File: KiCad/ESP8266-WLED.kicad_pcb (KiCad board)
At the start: 2 copper layers, 25.3 x 35.8 mm, 10 parts, among them J1 USB_C_Receptacle_USB2.0_14P, U1 ESP-12F

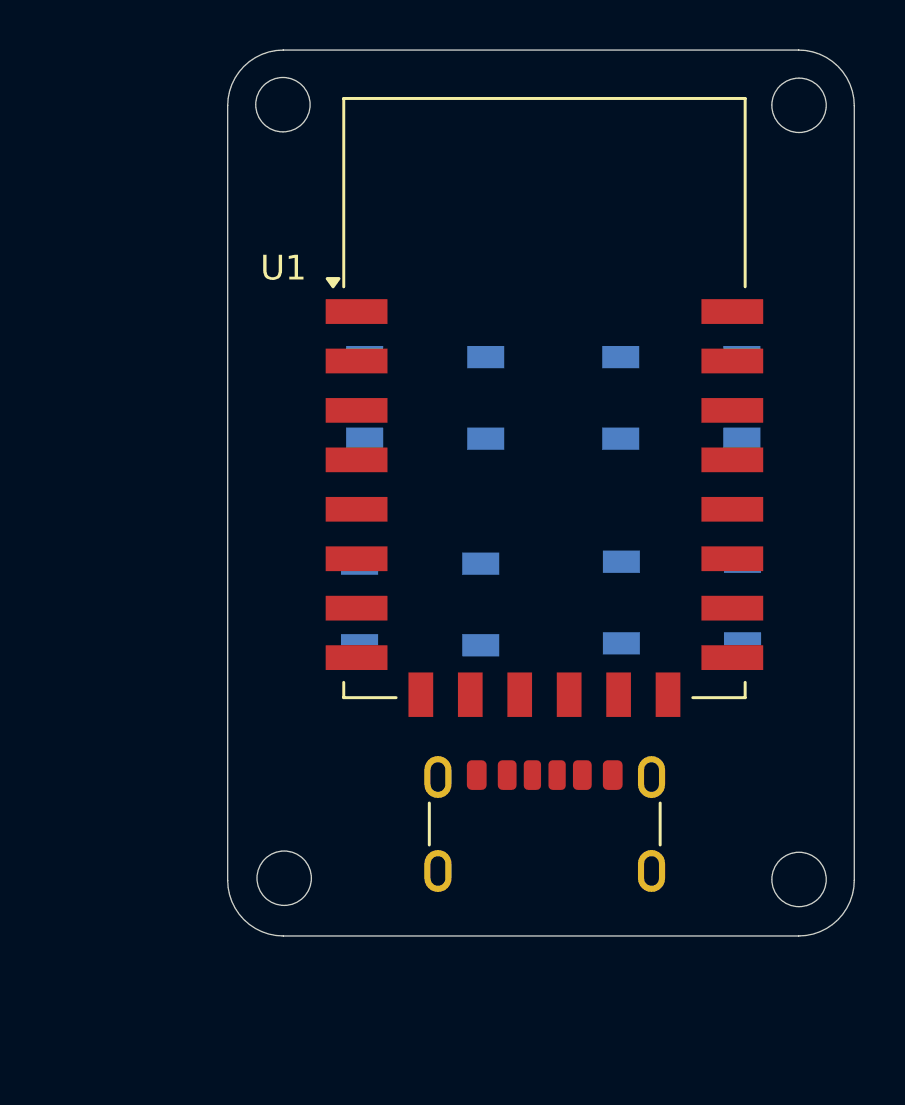
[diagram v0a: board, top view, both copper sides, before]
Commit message: adding power supply, etc.
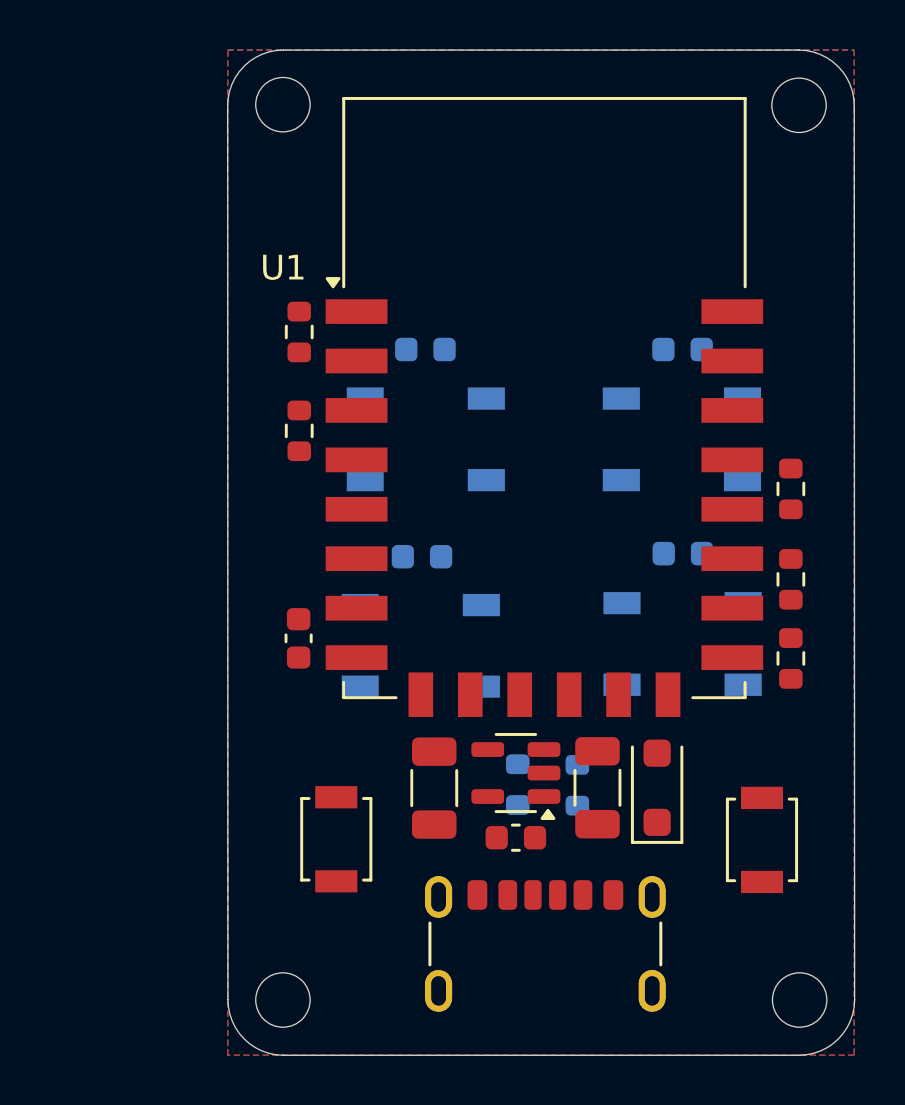
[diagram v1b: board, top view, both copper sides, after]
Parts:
- added C1: 100nF, Capacitor_SMD:C_0603_1608Metric, F.Cu at (140.1, 107.6)
- added C2: 100nF, Capacitor_SMD:C_0603_1608Metric, B.Cu at (155.6, 95.9)
- added C3: 100nF, Capacitor_SMD:C_0603_1608Metric, B.Cu at (155.6, 104.2)
- added C4: 100nF, Capacitor_SMD:C_0603_1608Metric, B.Cu at (145.0, 104.3)
- added C5: 100nF, Capacitor_SMD:C_0603_1608Metric, B.Cu at (145.2, 95.9)
- added C6: 10u, Capacitor_SMD:C_1206_3216Metric, F.Cu at (152.1, 113.6)
- added C7: 10u, Capacitor_SMD:C_1206_3216Metric, F.Cu at (145.5, 113.7)
- added C8: 470pF, Capacitor_SMD:C_0603_1608Metric, F.Cu at (148.8, 115.7)
- added D5: MBR120VLSFT1G, Diode_SMD:D_SOD-123F, F.Cu at (154.6, 113.6)
- added R1: 10K, Resistor_SMD:R_0603_1608Metric, F.Cu at (140.1, 95.2)
- added R2: 10K, Resistor_SMD:R_0603_1608Metric, F.Cu at (140.1, 99.2)
- added R3: 10K, Resistor_SMD:R_0603_1608Metric, F.Cu at (160.0, 101.5)
- added R4: 10K, Resistor_SMD:R_0603_1608Metric, F.Cu at (160.0, 105.2)
- added R5: 10K, Resistor_SMD:R_0603_1608Metric, F.Cu at (160.0, 108.4)
- added R6: 5k1, Resistor_SMD:R_0603_1608Metric, B.Cu at (148.9, 113.5)
- added R7: 5k1, Resistor_SMD:R_0603_1608Metric, B.Cu at (151.3, 113.5)
- added SW1: SW_Push, Button_Switch_SMD:SW_SPST_B3U-1000P, F.Cu at (141.6, 115.7)
- added SW2: SW_Push, Button_Switch_SMD:SW_SPST_B3U-1000P, F.Cu at (158.8, 115.7)
- added U2: MIC5219-3.3YM5, Package_TO_SOT_SMD:SOT-23-5, F.Cu at (148.8, 113.0)
- moved REF** 4.93 mm to (139.4, 122.2)
- moved REF** 4.88 mm to (160.3, 122.2)
- moved J1 4.85 mm to (150.0, 121.1)
- moved D1 1.68 mm to (155.6, 99.5)
- moved D4 1.68 mm to (145.0, 107.9)
- moved D2 1.68 mm to (145.2, 99.5)
- moved D3 1.68 mm to (155.6, 107.8)
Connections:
- D1 pad 1: unconnected-(D1-VDD-Pad1) -> +5V
- D1 pad 2: unconnected-(D1-DOUT-Pad2) -> Net-(D1-DOUT)
- D1 pad 3: unconnected-(D1-VSS-Pad3) -> GND
- D2 pad 1: unconnected-(D2-VDD-Pad1) -> +5V
- D2 pad 2: unconnected-(D2-DOUT-Pad2) -> Net-(D2-DOUT)
- D2 pad 3: unconnected-(D2-VSS-Pad3) -> GND
- D2 pad 4: unconnected-(D2-DIN-Pad4) -> Net-(D1-DOUT)
- D3 pad 1: unconnected-(D3-VDD-Pad1) -> +5V
- D3 pad 2: unconnected-(D3-DOUT-Pad2) -> Net-(D3-DOUT)
- D3 pad 3: unconnected-(D3-VSS-Pad3) -> GND
- D3 pad 4: unconnected-(D3-DIN-Pad4) -> Net-(D2-DOUT)
- D4 pad 1: unconnected-(D4-VDD-Pad1) -> +5V
- D4 pad 3: unconnected-(D4-VSS-Pad3) -> GND
- D4 pad 4: unconnected-(D4-DIN-Pad4) -> Net-(D3-DOUT)
- J1 pad A12: Net-(J1-GND-PadA1) -> GND
- J1 pad A5: unconnected-(J1-CC1-PadA5) -> Net-(J1-CC1)
- J1 pad B12: Net-(J1-GND-PadA1) -> GND
- J1 pad B5: unconnected-(J1-CC2-PadB5) -> Net-(J1-CC2)
- J1 pad S1: unconnected-(J1-SHIELD-PadS1) -> GND
- U1 pad 1: unconnected-(U1-~{RST}-Pad1) -> Net-(U1-~{RST})
- U1 pad 16: unconnected-(U1-GPIO15-Pad16) -> Net-(U1-GPIO15)
- U1 pad 17: unconnected-(U1-GPIO2-Pad17) -> Net-(U1-GPIO2)
- U1 pad 18: unconnected-(U1-GPIO0-Pad18) -> Net-(U1-GPIO0)
- U1 pad 3: unconnected-(U1-EN-Pad3) -> Net-(U1-EN)
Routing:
- added copper zone on B.Cu, net GND
- added copper zone on F.Cu, net GND
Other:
- board size 25.3 x 35.8 mm -> 25.4 x 40.7 mm

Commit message: adding serial interface
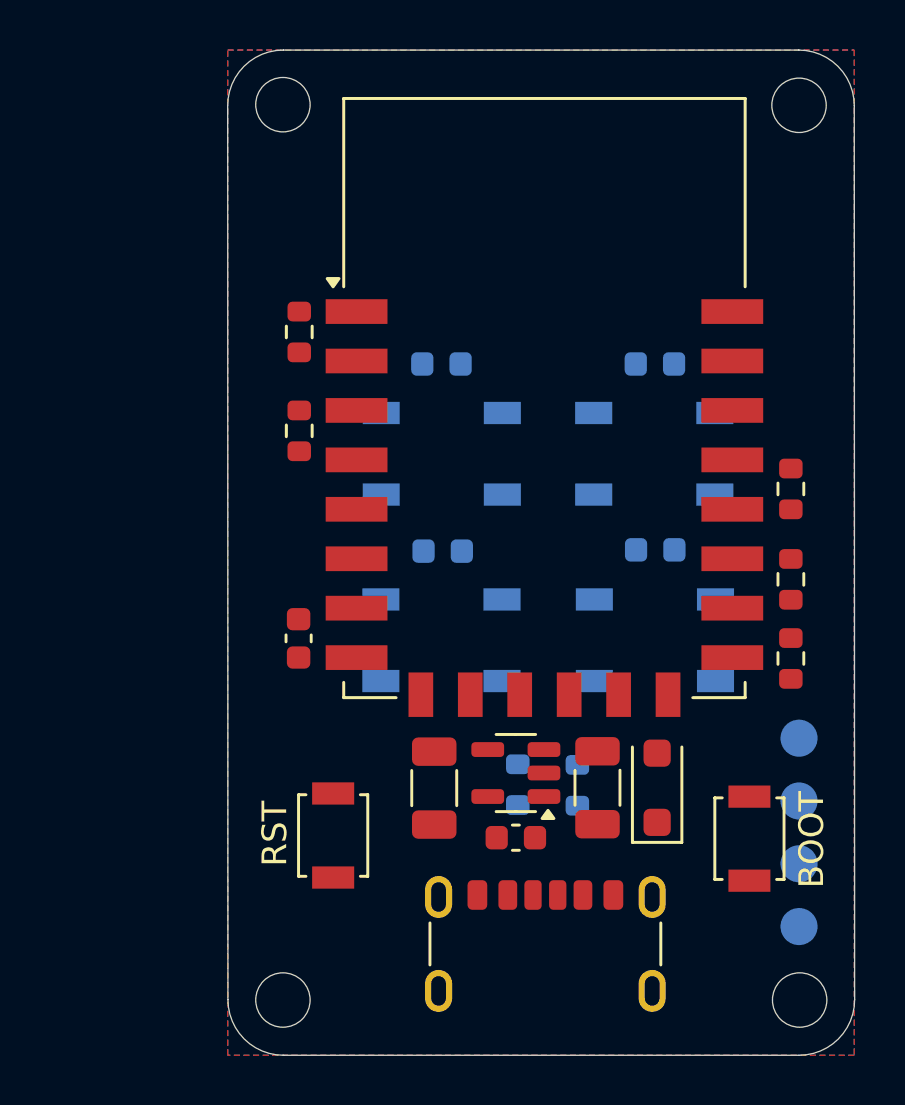
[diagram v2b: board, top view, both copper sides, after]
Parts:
- added J2: Conn_01x01_Socket, TestPoint:TestPoint_Pad_D1.5mm, B.Cu at (160.3, 111.6)
- added J3: Conn_01x01_Socket, TestPoint:TestPoint_Pad_D1.5mm, B.Cu at (160.3, 114.2)
- added J4: Conn_01x01_Socket, TestPoint:TestPoint_Pad_D1.5mm, B.Cu at (160.3, 116.7)
- added J5: Conn_01x01_Socket, TestPoint:TestPoint_Pad_D1.5mm, B.Cu at (160.3, 119.3)
- added REF**: OSHW-Logo2_7.3x6mm_SilkScreen, Symbol:OSHW-Logo2_7.3x6mm_SilkScreen, B.Cu at (141.2, 115.5)
- moved SW2 17.3 mm to (141.5, 115.6)
- moved SW1 16.7 mm to (158.3, 115.7)
- moved C2 1.26 mm to (154.5, 96.5)
- moved D1 1.26 mm to (154.4, 100.1)
- moved C3 1.13 mm to (154.5, 104.0)
- moved D3 1.13 mm to (154.5, 107.7)
- moved C5 0.87 mm to (145.8, 96.5)
- moved D2 0.87 mm to (145.8, 100.1)
- moved D4 0.87 mm to (145.8, 107.7)
- moved C4 0.87 mm to (145.9, 104.1)
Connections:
- SW1 pad 2: Net-(U1-EN) -> Net-(U1-GPIO0)
- U1 pad 21: unconnected-(U1-GPIO3/RXD-Pad21) -> /RXD
- U1 pad 22: unconnected-(U1-GPIO1/TXD-Pad22) -> /TXD
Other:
- board text added: "BOOT"
- board text added: "ESP8266-WLED"
- board text added: "GND"
- board text added: "RST"
- board text added: "RXD"
- board text added: "Rev 1.0 - 2024.09"
- board text added: "TXD"
- board text added: "VCC"

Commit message: updating README file
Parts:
- removed the REF** at (141.2, 115.5)

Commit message: first placement
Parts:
- moved C3 7.88 mm to (146.6, 104.0)
- moved C2 7.87 mm to (146.6, 96.4)
- moved D3 7.87 mm to (146.6, 107.6)
- moved J2 7.84 mm to (152.8, 109.5)
- moved D1 7.84 mm to (146.6, 100.0)
- moved J3 7.73 mm to (152.8, 112.5)
- moved R6 7.70 mm to (141.2, 112.8)
- moved J4 7.65 mm to (152.8, 115.5)
- moved R5 7.64 mm to (152.4, 107.6)
- moved R4 7.62 mm to (152.4, 104.5)
- moved R3 7.60 mm to (152.4, 101.4)
- moved R7 7.59 mm to (143.8, 112.9)
- moved SW1 7.59 mm to (150.7, 115.0)
- moved SW2 7.59 mm to (133.9, 114.9)
- moved J5 7.59 mm to (152.8, 118.5)
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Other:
- board size 25.4 x 40.7 mm -> 25 x 40 mm
- board text added: "https://github.com/dokuhn/ESP8266-WLED"

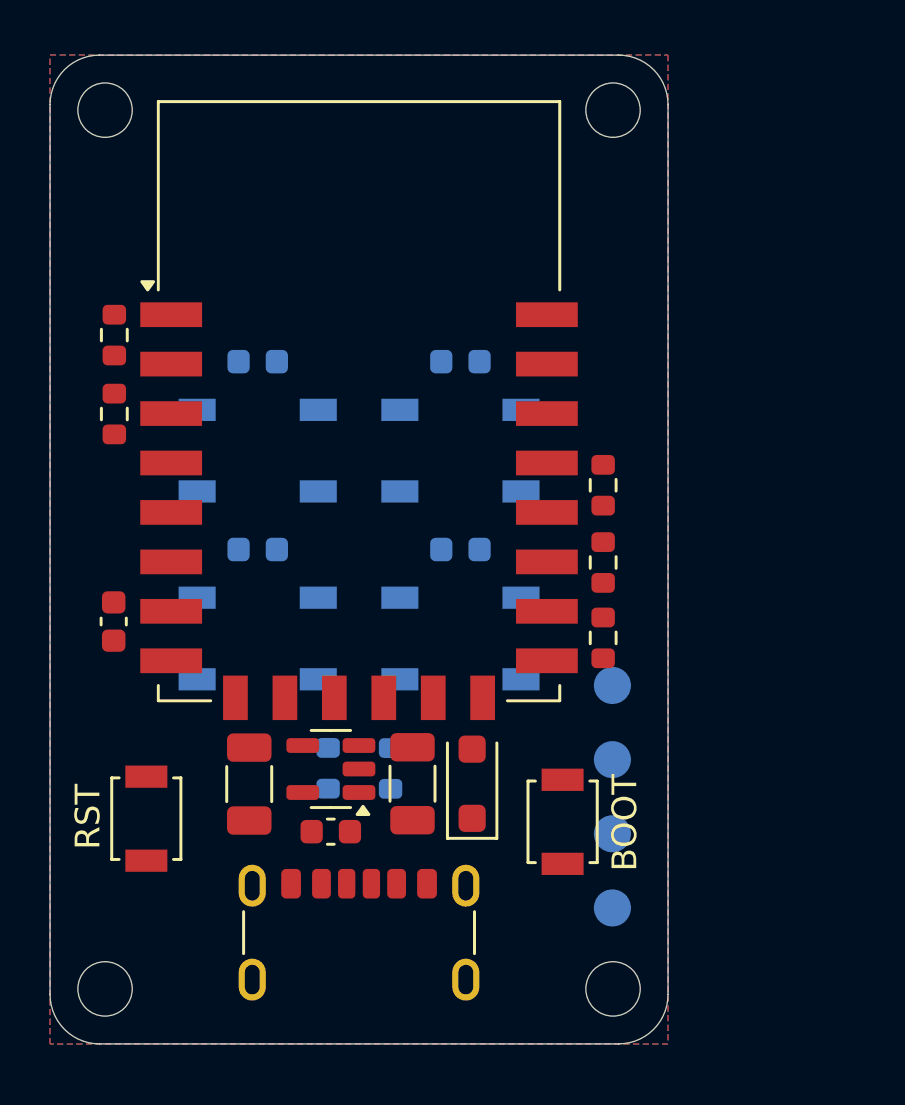
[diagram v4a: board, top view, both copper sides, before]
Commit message: first traces routed
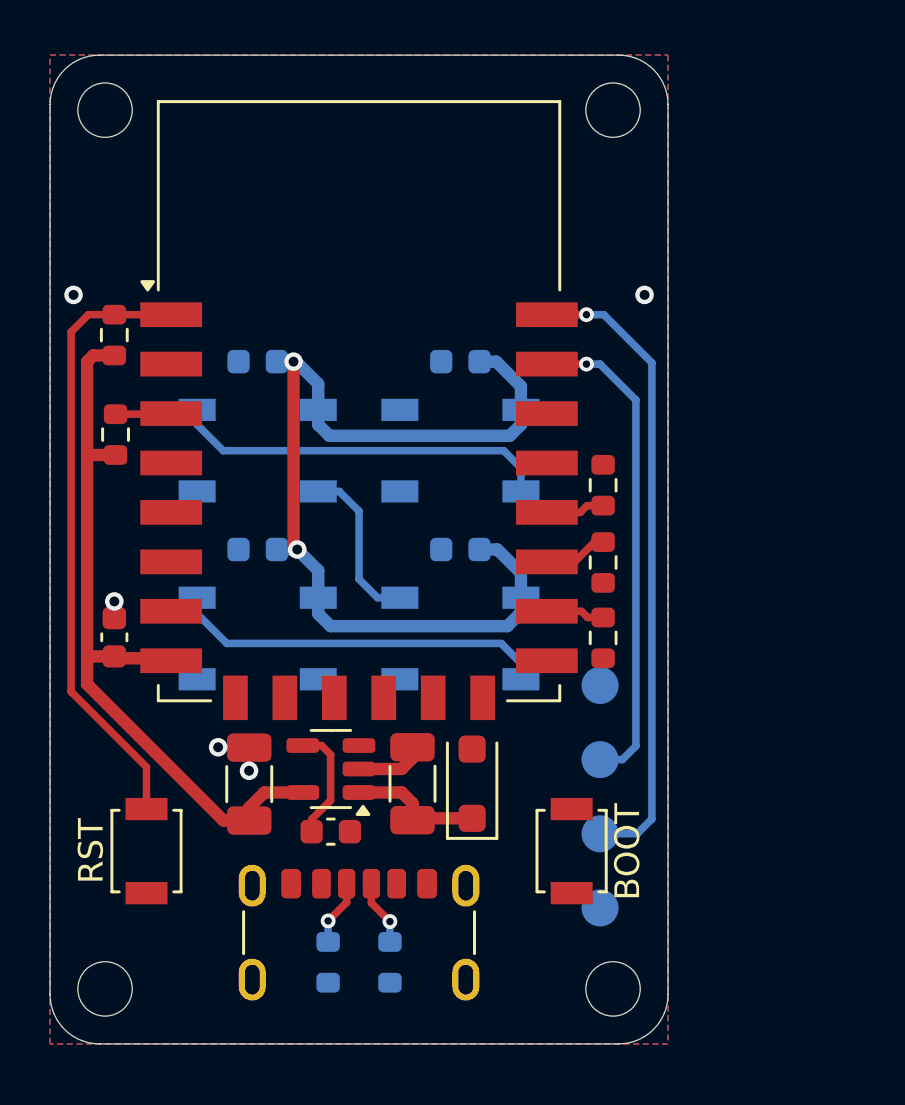
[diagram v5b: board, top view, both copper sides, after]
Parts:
- moved R6 7.85 mm to (141.2, 120.7), turned to -90 degrees
- moved R7 7.84 mm to (143.8, 120.7), turned to -90 degrees
- moved SW2 1.31 mm to (133.9, 116.2)
- moved SW1 1.24 mm to (151.1, 116.2)
- moved R2 0.83 mm to (132.7, 99.3)
- moved C1 0.64 mm to (132.6, 107.5)
- moved J2 0.50 mm to (152.2, 109.5)
- moved J3 0.50 mm to (152.2, 112.5)
- moved J4 0.50 mm to (152.2, 115.5)
- moved J5 0.50 mm to (152.2, 118.5)
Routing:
- net +5V: track 0.00 -> 45.1 mm, vias 0 -> 2
- net +3V3: track 0.00 -> 30.9 mm
- net /TXD: track 0.00 -> 25.9 mm, vias 0 -> 1
- net Net-(U1-~{RST}): track 0.00 -> 24.9 mm
- net /RXD: track 0.00 -> 19.9 mm, vias 0 -> 1
- net Net-(D1-DOUT): track 0.00 -> 15.4 mm
- net Net-(D3-DOUT): track 0.00 -> 15.2 mm
- net Net-(D2-DOUT): track 0.00 -> 6.69 mm
- net Net-(U2-BP): track 0.00 -> 4.71 mm
- net GND: track 0.00 -> 2.79 mm, vias 0 -> 5
- net Net-(J1-CC2): track 0.00 -> 2.67 mm, vias 0 -> 1
- net Net-(J1-CC1): track 0.00 -> 2.67 mm, vias 0 -> 1
- net Net-(U1-GPIO2): track 0.00 -> 2.61 mm
- net Net-(U1-GPIO0): track 0.00 -> 2.39 mm
- net Net-(U1-GPIO15): track 0.00 -> 2.38 mm
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
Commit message: first time everything routed
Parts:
- removed D5: MBR120VLSFT1G, Diode_SMD:D_SOD-123F
- moved C6 1.14 mm to (145.8, 113.5)
- moved C7 1.14 mm to (139.2, 113.5)
- moved U2 1.14 mm to (142.5, 112.9)
- moved C8 1.14 mm to (142.5, 115.4)
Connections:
- D1 pad 4: unconnected-(D1-DIN-Pad4) -> /DIN
- J1 pad A9: Net-(D5-A) -> +5V
- J1 pad B9: Net-(D5-A) -> +5V
- U1 pad 19: unconnected-(U1-GPIO4-Pad19) -> /DIN
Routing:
- net +3V3: track 30.9 -> 60.4 mm, vias 0 -> 2
- net +5V: track 45.1 -> 66.3 mm, vias 2 -> 3
- net Net-(U1-GPIO0): track 2.39 -> 16.8 mm
- net /DIN: track 0.00 -> 6.86 mm, vias 0 -> 1
- net Net-(U1-GPIO2): track 2.61 -> 1.13 mm
- net GND: track 2.79 -> 3.04 mm, vias 5 -> 15

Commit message: making some fine-tuning of the PCB
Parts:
- moved SW1 0.11 mm to (151.0, 116.2)
- moved SW2 0.11 mm to (134.0, 116.2)
- moved R6 0.05 mm to (141.2, 120.6)
- moved R7 0.05 mm to (143.8, 120.6)
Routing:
- net GND: track 3.04 -> 3.15 mm, vias 15 -> 24
